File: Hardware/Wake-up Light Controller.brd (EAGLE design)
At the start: 85.7 x 54 mm, 46 parts, among them IC1 ST1S10, IC2 HT7333, IC3 DS3231/SO, IC4 ATMEGA328P_TQFP, J1 AVR-ISP, J2 Debug, Q1 BSS138, Q2 BSS138, Q3 FDN306P, Q4 IRLZ44N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

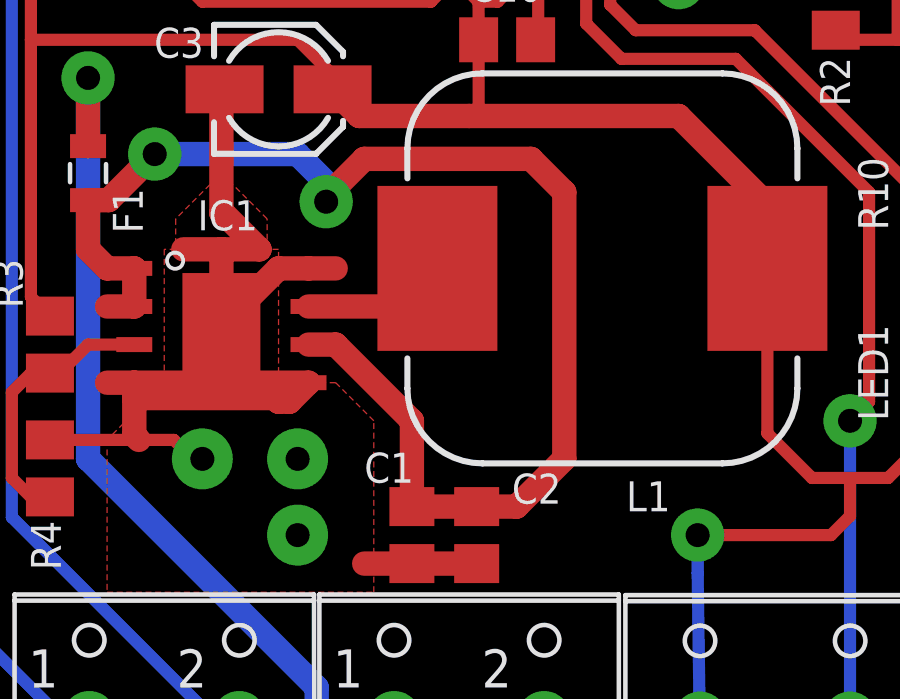
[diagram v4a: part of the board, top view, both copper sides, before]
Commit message: Modify copper trace
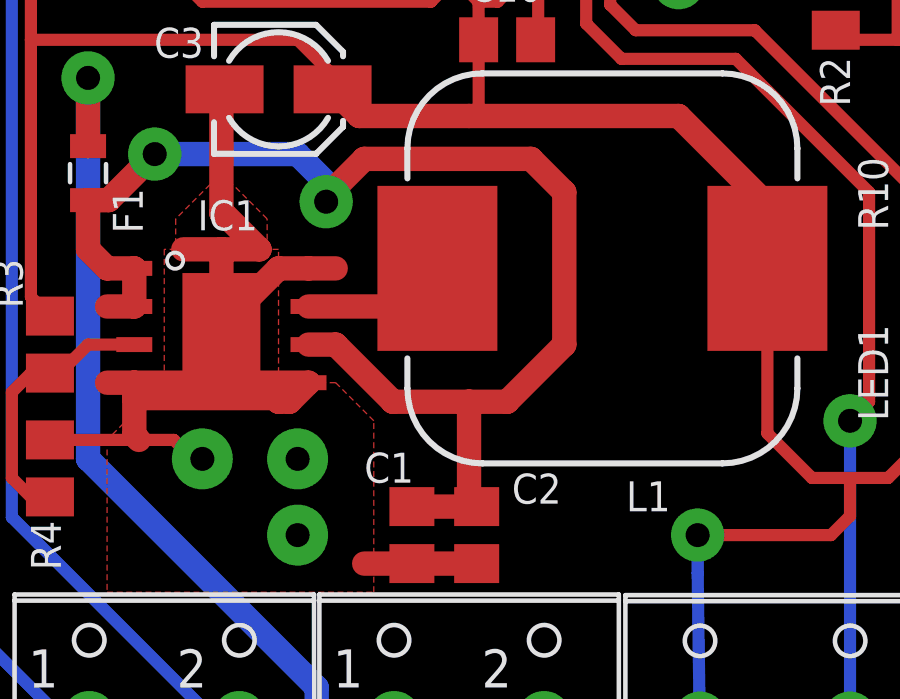
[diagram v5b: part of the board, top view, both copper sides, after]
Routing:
- net N$9: track 46.6 -> 45.4 mm
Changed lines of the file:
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@@
 <wire x1="9.161" y1="20.32" x2="8.255" y2="20.32" width="0.8128" layer="1"/>
 <wire x1="9.161" y1="21.59" x2="9.161" y2="20.32" width="0.8128" layer="1"/>
-<wire x1="18.415" y1="16.51" x2="18.415" y2="13.65" width="0.8128" layer="1"/>
-<wire x1="18.415" y1="16.51" x2="15.875" y2="19.05" width="0.8128" layer="1"/>
+<wire x1="17.78" y1="17.145" x2="15.875" y2="19.05" width="0.8128" layer="1"/>
 <wire x1="15.875" y1="19.05" x2="14.969" y2="19.05" width="0.8128" layer="1"/>
 <contactref element="F1" pad="2"/>
@@
 <wire x1="16.8275" y1="25.24125" x2="22.38375" y2="25.24125" width="0.8128" layer="1"/>
 <wire x1="22.38375" y1="25.24125" x2="23.495" y2="24.13" width="0.8128" layer="1"/>
-<wire x1="23.495" y1="15.24" x2="23.495" y2="24.13" width="0.8128" layer="1"/>
-<wire x1="20.574" y1="13.65" x2="21.905" y2="13.65" width="0.8128" layer="1"/>
-<wire x1="21.905" y1="13.65" x2="23.495" y2="15.24" width="0.8128" layer="1"/>
+<wire x1="23.495" y1="19.05" x2="23.495" y2="24.13" width="0.8128" layer="1"/>
 <wire x1="7.62" y1="22.225" x2="7.62" y2="23.865" width="0.8128" layer="1"/>
 <wire x1="7.62" y1="22.225" x2="8.255" y2="21.59" width="0.8128" layer="1"/>
@@
 <wire x1="8.3075" y1="23.865" x2="9.8425" y2="25.4" width="0.8128" layer="1"/>
 <wire x1="7.62" y1="23.865" x2="8.3075" y2="23.865" width="0.8128" layer="1"/>
-<wire x1="18.415" y1="13.65" x2="20.574" y2="13.65" width="0.8128" layer="1"/>
+<wire x1="20.32" y1="13.65" x2="18.415" y2="13.65" width="0.8128" layer="1"/>
+<wire x1="20.32" y1="13.65" x2="20.574" y2="13.65" width="0.8128" layer="1"/>
+<wire x1="23.495" y1="19.05" x2="21.59" y2="17.145" width="0.8128" layer="1"/>
+<wire x1="21.59" y1="17.145" x2="20.32" y2="17.145" width="0.8128" layer="1"/>
+<wire x1="20.32" y1="17.145" x2="17.78" y2="17.145" width="0.8128" layer="1"/>
+<wire x1="20.32" y1="17.145" x2="20.32" y2="13.65" width="0.8128" layer="1"/>
 </signal>
 </signals>

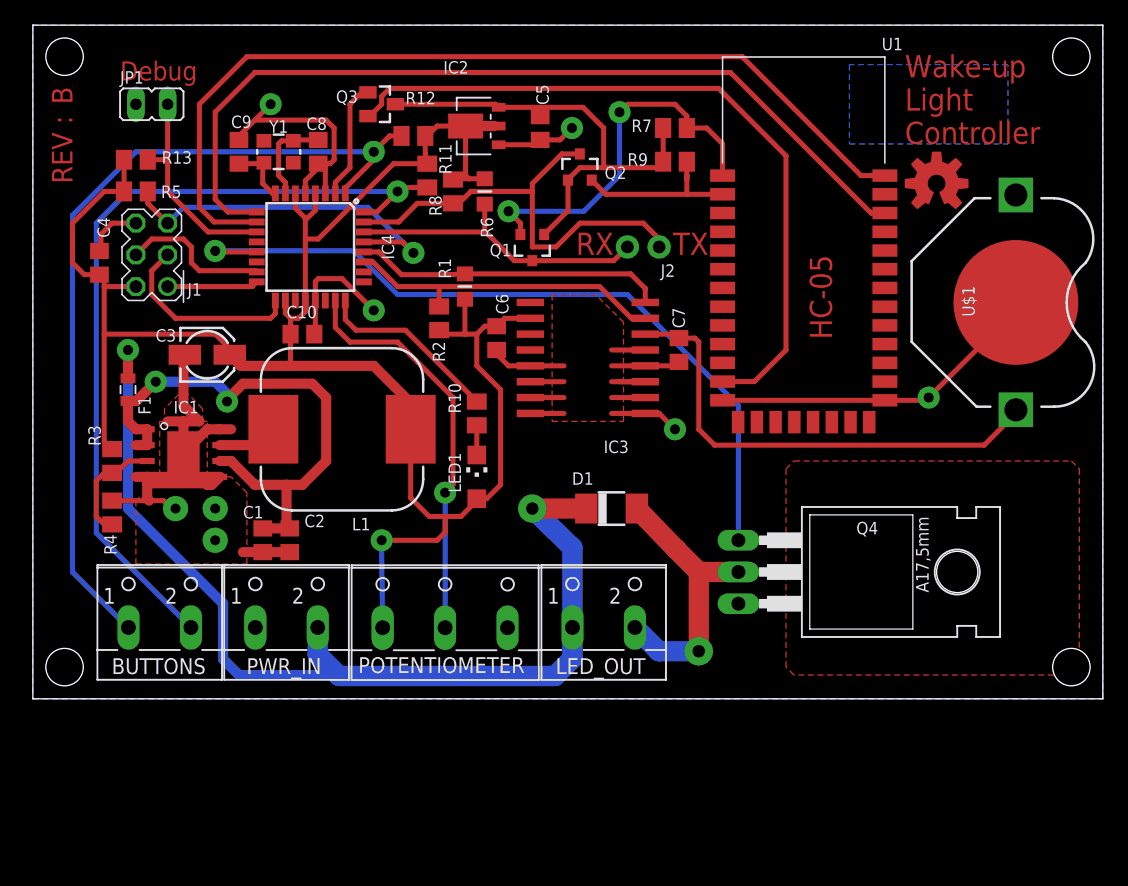
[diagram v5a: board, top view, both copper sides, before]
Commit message: Add overvoltage protection
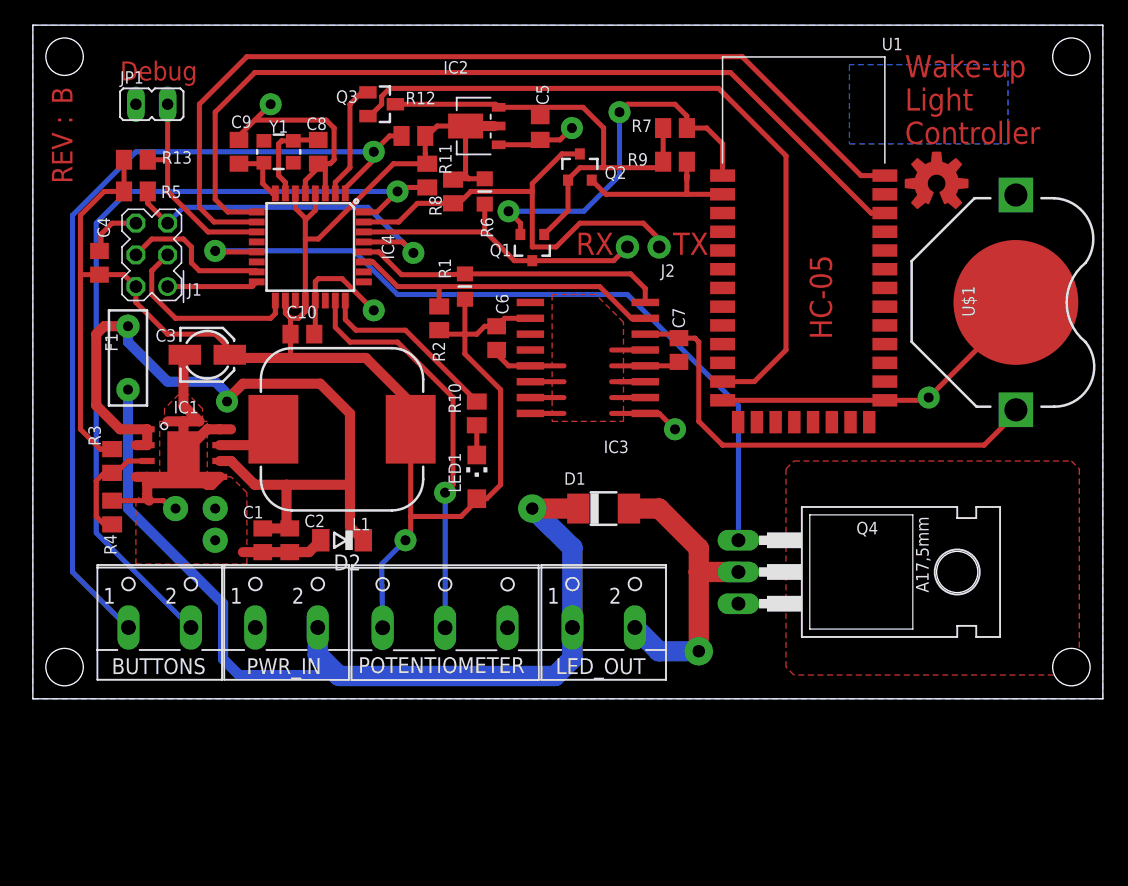
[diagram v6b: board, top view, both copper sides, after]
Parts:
- added D2: Zener 15v, diode:SOD80C
- F1: value PTC 500mA -> 30V/0.5A; device BaseApp:0805-METRIC -> SparkFun-Fuses:PTH
- moved F1 2.54 mm to (7.62, 27.3), turned to 90 degrees
- moved D1 0.63 mm to (45.7, 15.2)
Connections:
- net +12V: now also F1.P$1; no longer F1.1
- net GND: now also D2.A
- net N$9: now also D2.C, F1.P$2; no longer F1.2
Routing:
- net N$9: track 45.4 -> 66.4 mm, vias 2 -> 1
- net +12V: track 81.6 -> 75.5 mm, vias 2 -> 1
- net GND: track 142.2 -> 145.1 mm
- net N$1: track 22.5 -> 24.2 mm
- net +5V: track 159.9 -> 158.2 mm

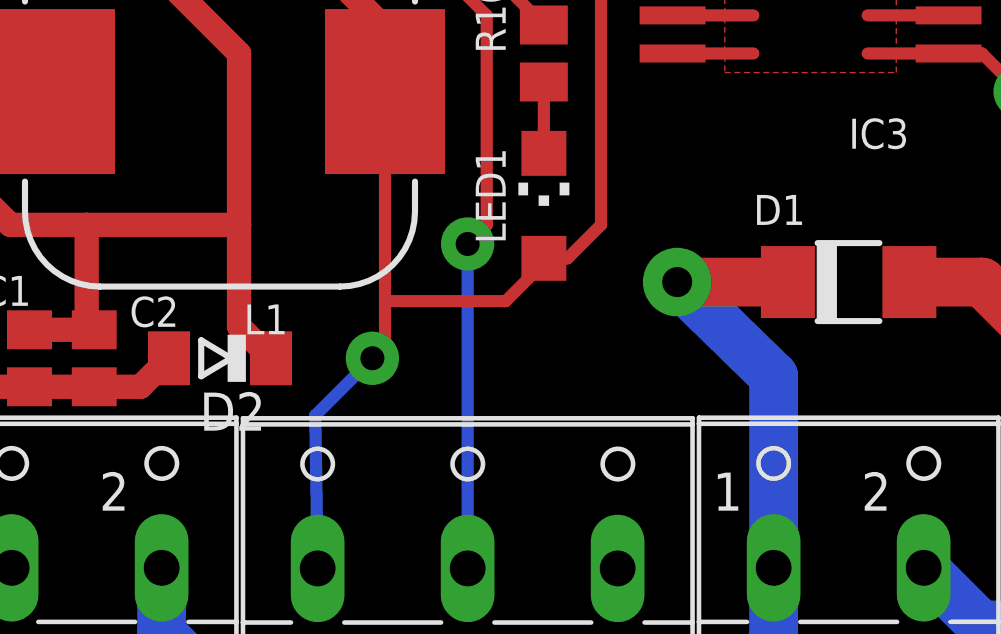
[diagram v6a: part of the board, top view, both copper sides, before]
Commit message: Change diodes names
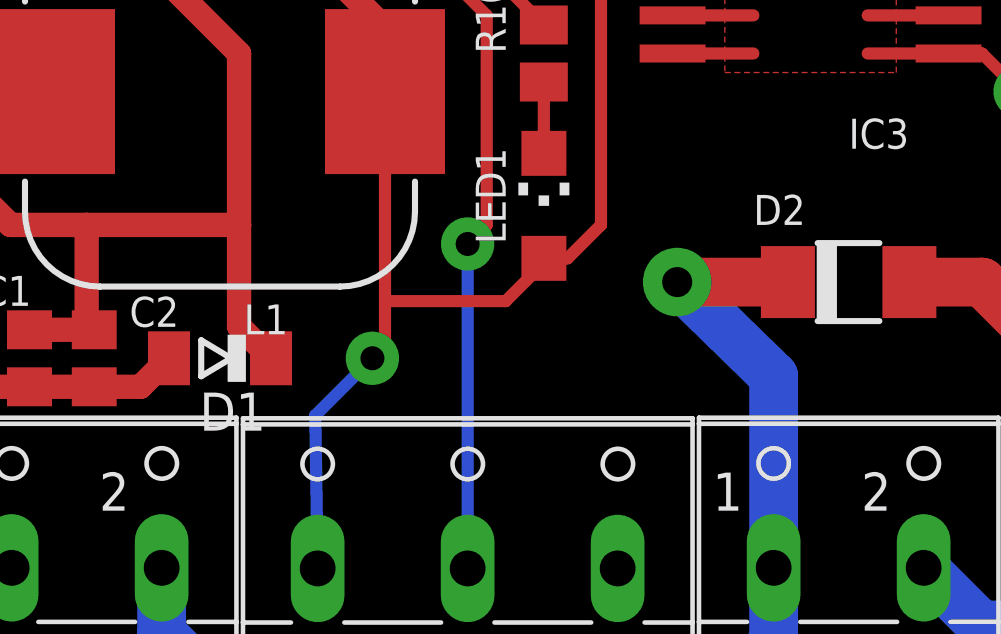
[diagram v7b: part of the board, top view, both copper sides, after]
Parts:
- D1: value 1N4004 -> Zener 15v; device diode:DO-214AC -> diode:SOD80C
- D2: value Zener 15v -> 1N4004; device diode:SOD80C -> diode:DO-214AC
- moved D1 21.1 mm to (24.8, 12.7), turned to 180 degrees
- moved D2 21.1 mm to (45.7, 15.2), turned to 0 degrees
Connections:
- net +12V: now also D2.C; no longer D1.C
- net GND: now also D1.A; no longer D2.A
- net N$1: now also D2.A; no longer D1.A
- net N$9: now also D1.C; no longer D2.C
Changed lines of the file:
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@@
 <attribute name="VALUE" x="14.44625" y="45.085" size="1" layer="27" rot="R270"/>
 </element>
-<element name="D1" library="diode" library_urn="urn:adsk.eagle:library:210" package="DO-214AC" package3d_urn="urn:adsk.eagle:package:43416/2" value="1N4004" x="45.72" y="15.24" smashed="yes">
+<element name="D2" library="diode" library_urn="urn:adsk.eagle:library:210" package="DO-214AC" package3d_urn="urn:adsk.eagle:package:43416/2" value="1N4004" x="45.72" y="15.24" smashed="yes">
 <attribute name="NAME" x="42.545" y="17.145" size="1" layer="25"/>
 <attribute name="VALUE" x="45.085" y="17.145" size="1" layer="27"/>
@@
 <attribute name="VALUE" value="72V/0.25A" x="9.652" y="23.114" size="1" layer="27" rot="R90"/>
 </element>
-<element name="D2" library="diode" library_urn="urn:adsk.eagle:library:210" package="SOD80C" package3d_urn="urn:adsk.eagle:package:43405/2" value="Zener 15v" x="24.765" y="12.7" rot="R180"/>
+<element name="D1" library="diode" library_urn="urn:adsk.eagle:library:210" package="SOD80C" package3d_urn="urn:adsk.eagle:package:43405/2" value="Zener 15v" x="24.765" y="12.7" rot="R180"/>
 </elements>
 <signals>
@@
 <wire x1="68.245" y1="23.91" x2="71.535" y2="23.91" width="0.4064" layer="1"/>
 <wire x1="71.535" y1="23.91" x2="71.755" y2="24.13" width="0.4064" layer="1"/>
-<contactref element="D2" pad="A"/>
+<contactref element="D1" pad="A"/>
 <wire x1="20.574" y1="11.75" x2="22.115" y2="11.75" width="0.8128" layer="1"/>
 <wire x1="22.115" y1="11.75" x2="23.065" y2="12.7" width="0.8128" layer="1"/>
 </signal>
 <signal name="+12V">
-<contactref element="D1" pad="C"/>
+<contactref element="D2" pad="C"/>
 <contactref element="LED_OUT" pad="1"/>
 <contactref element="PWR_IN" pad="2"/>
@@
 </signal>
 <signal name="N$1">
-<contactref element="D1" pad="A"/>
+<contactref element="D2" pad="A"/>
 <contactref element="LED_OUT" pad="2"/>
 <contactref element="Q4" pad="D"/>
@@
 <wire x1="20.32" y1="17.145" x2="17.78" y2="17.145" width="0.8128" layer="1"/>
 <wire x1="20.32" y1="17.145" x2="20.32" y2="13.65" width="0.8128" layer="1"/>
-<contactref element="D2" pad="C"/>
+<contactref element="D1" pad="C"/>
 <wire x1="23.01875" y1="25.24125" x2="25.4" y2="22.86" width="0.8128" layer="1"/>
 <wire x1="25.4" y1="17.145" x2="25.4" y2="22.86" width="0.8128" layer="1"/>
